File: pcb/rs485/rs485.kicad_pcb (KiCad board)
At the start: 2 copper layers, 67 x 49 mm, 28 parts, among them J1 Power, J2 Conn_01x05, J3 Conn_01x02, J4 Conn_01x02, J5 Conn_01x02, U1 SP485CN-L_TR, U2 ACT4065A

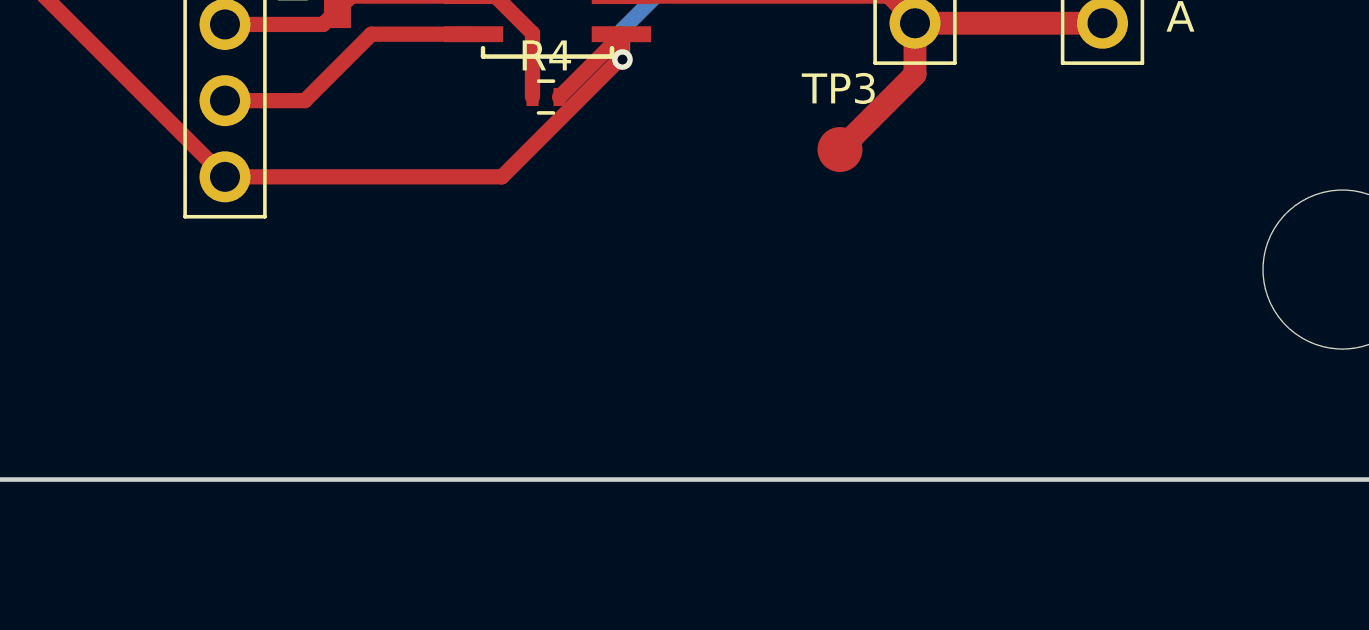
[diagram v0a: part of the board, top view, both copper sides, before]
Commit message: Add silkscreen name
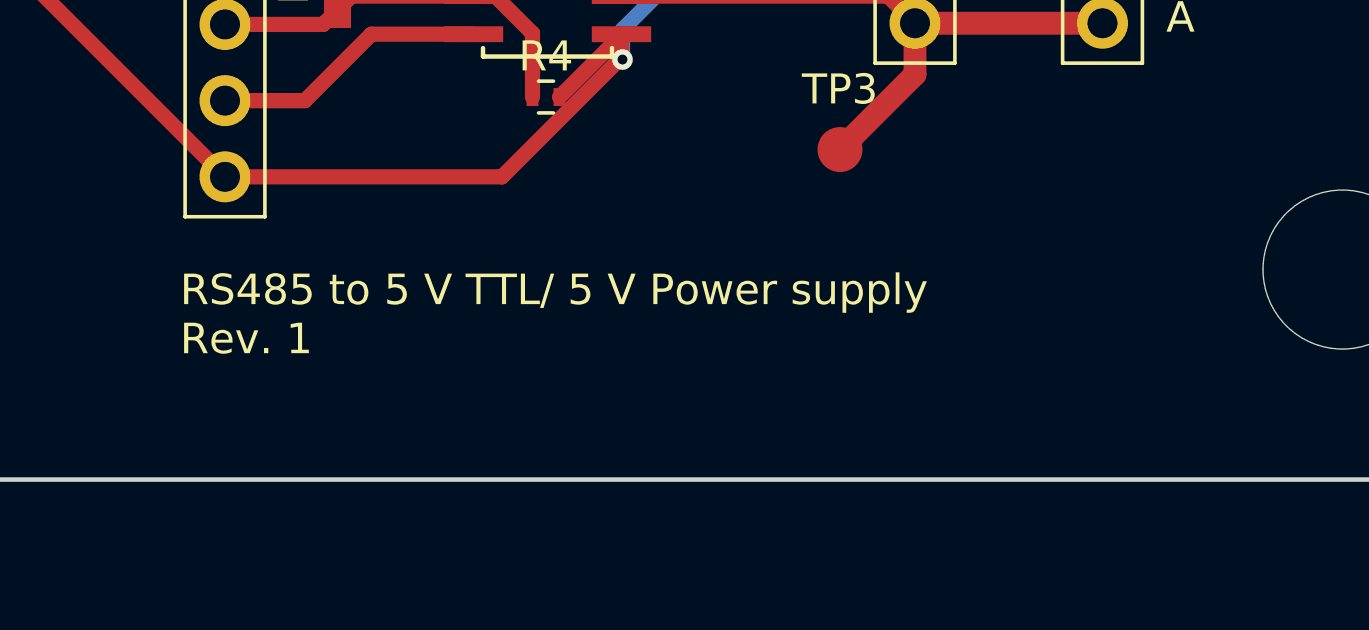
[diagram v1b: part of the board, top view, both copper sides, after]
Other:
- board text added: "RS485 to 5 V TTL/ 5 V Power supply Rev. 1"
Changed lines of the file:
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@@
   (general
     (thickness 1.6)
-    (drawings 7)
+    (drawings 8)
     (tracks 175)
     (zones 0)
@@
   )
   (setup
-    (last_trace_width 0.3302)
+    (last_trace_width 0.254)
     (user_trace_width 0.1524)
     (user_trace_width 0.254)
@@
       (net 1 GND))
   )
+  (gr_text "RS485 to 5 V TTL/ 5 V Power supply\nRev. 1" (at 49.25 114.5) (layer F.SilkS)
+    (effects (font (size 1.016 1.016) (thickness 0.1524)) (justify left))
+  )
   (gr_text A (at 82.6 104.6) (layer F.SilkS)

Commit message: Generate BOMs
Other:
- board size 67 x 49 mm -> 66 x 49 mm
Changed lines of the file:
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@@
   )
   (gr_line (start 29 120) (end 29 71) (layer Edge.Cuts) (width 0.1524))
-  (gr_line (start 95 120) (end 28 120) (layer Edge.Cuts) (width 0.1524))
+  (gr_line (start 95 120) (end 29 120) (layer Edge.Cuts) (width 0.1524))
   (gr_line (start 95 71) (end 95 120) (layer Edge.Cuts) (width 0.1524))
   (gr_line (start 29 71) (end 95 71) (layer Edge.Cuts) (width 0.1524))
